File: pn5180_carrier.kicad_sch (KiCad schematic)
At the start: 35 parts, among them J1 Bay 0 (CLIK-Mate 1x10), J10 24V IN (CLIK-Mate 1x2), J2 Bay 1 (CLIK-Mate 1x10), J3 Bay 2 (CLIK-Mate 1x10), J4 Bay 3 (CLIK-Mate 1x10), J5 Bay 4 (CLIK-Mate 1x10), J6 Bay 5 (CLIK-Mate 1x10), J7 Bay 6 (CLIK-Mate 1x10), J8 Bay 7 (CLIK-Mate 1x10), U1 74HC138, U2 74HC151, U4 TLV1117LV33DCYR, U5 XIAO ESP32C6, U6 MP1584EN module (set 5.0V)

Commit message: Bay connectors J1-J8: CLIK-Mate 1.50 mm dual-row 2x5 (503148-1090), rev 1.4
- New project footprint carrier:Molex_CLIK-Mate_503148-1090_2x05-1MP_P1.50mm_Horizontal
  from Molex's catalog drawing (10 pads 0.55x2.70 at 0.75 mm in one line at the rear,
  nail pads 1.20x4.65 at the front corners, body 11.8x8.75). Nail-pad fore-aft position
  and the sequential pad order are to be confirmed on SD-503148-1090.
- Schematic: J1-J8 footprint/MPN/Mouser/description/value fields, DESIGN NOTES text,
  title-block rev 1.3 -> 1.4. Netlist (38 nets, 189 nodes, 0 problems) and ERC unchanged.
- BOM CSV and Mouser order list: 503148-1090 x8, housing 503149-1000 x8, terminals
  502579-0000 cut strip of 100; the 24 V cable stays on the 2.00 mm family.
- README, CLAUDE.md, MEMORY.md: connector, harness (24-28 AWG thin-wall), stock check,
  layout consequences; PCB footprint swap and re-layout recorded as open item 12.

Co-Authored-By: Claude Fable 5.1 <noreply@anthropic.com>
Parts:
- J1: value Bay 0 (CLIK-Mate 1x10) -> Bay 0 (CLIK-Mate 2x5); footprint Connector_Molex:Molex_CLIK-Mate_502494-1070_1x10-1MP_P2.00mm_Horizontal -> carrier:Molex_CLIK-Mate_503148-1090_2x05-1MP_P1.50mm_Horizontal; MPN 502494-1070 -> 503148-1090; Mouser 538-502494-1070 -> 538-503148-1090
- J2: value Bay 1 (CLIK-Mate 1x10) -> Bay 1 (CLIK-Mate 2x5); footprint Connector_Molex:Molex_CLIK-Mate_502494-1070_1x10-1MP_P2.00mm_Horizontal -> carrier:Molex_CLIK-Mate_503148-1090_2x05-1MP_P1.50mm_Horizontal; MPN 502494-1070 -> 503148-1090; Mouser 538-502494-1070 -> 538-503148-1090
- J3: value Bay 2 (CLIK-Mate 1x10) -> Bay 2 (CLIK-Mate 2x5); footprint Connector_Molex:Molex_CLIK-Mate_502494-1070_1x10-1MP_P2.00mm_Horizontal -> carrier:Molex_CLIK-Mate_503148-1090_2x05-1MP_P1.50mm_Horizontal; MPN 502494-1070 -> 503148-1090; Mouser 538-502494-1070 -> 538-503148-1090
- J4: value Bay 3 (CLIK-Mate 1x10) -> Bay 3 (CLIK-Mate 2x5); footprint Connector_Molex:Molex_CLIK-Mate_502494-1070_1x10-1MP_P2.00mm_Horizontal -> carrier:Molex_CLIK-Mate_503148-1090_2x05-1MP_P1.50mm_Horizontal; MPN 502494-1070 -> 503148-1090; Mouser 538-502494-1070 -> 538-503148-1090
- J5: value Bay 4 (CLIK-Mate 1x10) -> Bay 4 (CLIK-Mate 2x5); footprint Connector_Molex:Molex_CLIK-Mate_502494-1070_1x10-1MP_P2.00mm_Horizontal -> carrier:Molex_CLIK-Mate_503148-1090_2x05-1MP_P1.50mm_Horizontal; MPN 502494-1070 -> 503148-1090; Mouser 538-502494-1070 -> 538-503148-1090
- J6: value Bay 5 (CLIK-Mate 1x10) -> Bay 5 (CLIK-Mate 2x5); footprint Connector_Molex:Molex_CLIK-Mate_502494-1070_1x10-1MP_P2.00mm_Horizontal -> carrier:Molex_CLIK-Mate_503148-1090_2x05-1MP_P1.50mm_Horizontal; MPN 502494-1070 -> 503148-1090; Mouser 538-502494-1070 -> 538-503148-1090
- J7: value Bay 6 (CLIK-Mate 1x10) -> Bay 6 (CLIK-Mate 2x5); footprint Connector_Molex:Molex_CLIK-Mate_502494-1070_1x10-1MP_P2.00mm_Horizontal -> carrier:Molex_CLIK-Mate_503148-1090_2x05-1MP_P1.50mm_Horizontal; MPN 502494-1070 -> 503148-1090; Mouser 538-502494-1070 -> 538-503148-1090
- J8: value Bay 7 (CLIK-Mate 1x10) -> Bay 7 (CLIK-Mate 2x5); footprint Connector_Molex:Molex_CLIK-Mate_502494-1070_1x10-1MP_P2.00mm_Horizontal -> carrier:Molex_CLIK-Mate_503148-1090_2x05-1MP_P1.50mm_Horizontal; MPN 502494-1070 -> 503148-1090; Mouser 538-502494-1070 -> 538-503148-1090
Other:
- note added: "All SMD except the XIAO sockets and U6's four THT pads. Bays: Molex CLIK-Mate 1.50mm dual-row RA receptacles 503148-1090 (2x5), housings 503149-1000, terminals 502579 (24-28 AWG). J10: CLIK-Mate 2.00mm 502494-0270, housing 502439-0200, terminals 502438."
- note removed: "All SMD except the XIAO sockets. Connectors: Molex CLIK-Mate 2.00mm RA receptacles (502494-xx70), housings 502439-xx00, terminals 502438."
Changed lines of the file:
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@@
 		(title "PN5180 8-Bay NFC Reader Carrier")
 		(date "2026-09-04")
-		(rev "1.3")
+		(rev "1.4")
 		(company "hyiger")
 		(comment 1 "74HC138 chip-select decoder + 74HC151 BUSY mux, 5 ESP32 GPIOs for 8 readers")
@@
 		)
 	)
-	(text "All SMD except the XIAO sockets. Connectors: Molex CLIK-Mate 2.00mm RA receptacles (502494-xx70), housings 502439-xx00, terminals 502438."
+	(text "All SMD except the XIAO sockets and U6's four THT pads. Bays: Molex CLIK-Mate 1.50mm dual-row RA receptacles 503148-1090 (2x5), housings 503149-1000, terminals 502579 (24-28 AWG). J10: CLIK-Mate 2.00mm 502494-0270, housing 502439-0200, terminals 502438."
 		(exclude_from_sim no)
 		(at 243.84 226.06 0)
@@
 			)
 		)
-		(property "Value" "Bay 1 (CLIK-Mate 1x10)"
+		(property "Value" "Bay 1 (CLIK-Mate 2x5)"
 			(at 266.7 95.885 0)
 			(show_name no)
@@
 			)
 		)
-		(property "Footprint" "Connector_Molex:Molex_CLIK-Mate_502494-1070_1x10-1MP_P2.00mm_Horizontal"
+		(property "Footprint" "carrier:Molex_CLIK-Mate_503148-1090_2x05-1MP_P1.50mm_Horizontal"
 			(at 269.24 81.28 0)
 			(hide yes)
@@
 			)
 		)
-		(property "Description" "CLIK-Mate 2.00mm RA SMT receptacle 1x10, positive lock"
+		(property "Description" "CLIK-Mate 1.50mm dual-row RA SMT receptacle 2x5, positive lock"
 			(at 269.24 81.28 0)
 			(hide yes)
@@
 			)
 		)
-		(property "MPN" "502494-1070"
+		(property "MPN" "503148-1090"
 			(at 269.24 81.28 0)
 			(hide yes)
@@
 			)
 		)
-		(property "Mouser" "538-502494-1070"
+		(property "Mouser" "538-503148-1090"
 			(at 269.24 81.28 0)
 			(hide yes)
@@
 			)
 		)
-		(property "Value" "Bay 5 (CLIK-Mate 1x10)"
+		(property "Value" "Bay 5 (CLIK-Mate 2x5)"
 			(at 353.06 95.885 0)
 			(show_name no)
@@
 			)
 		)
-		(property "Footprint" "Connector_Molex:Molex_CLIK-Mate_502494-1070_1x10-1MP_P2.00mm_Horizontal"
+		(property "Footprint" "carrier:Molex_CLIK-Mate_503148-1090_2x05-1MP_P1.50mm_Horizontal"
 			(at 355.6 81.28 0)
 			(hide yes)
@@
 			)
 		)
-		(property "Description" "CLIK-Mate 2.00mm RA SMT receptacle 1x10, positive lock"
+		(property "Description" "CLIK-Mate 1.50mm dual-row RA SMT receptacle 2x5, positive lock"
 			(at 355.6 81.28 0)
 			(hide yes)
@@
 			)
 		)
-		(property "MPN" "502494-1070"
+		(property "MPN" "503148-1090"
 			(at 355.6 81.28 0)
 			(hide yes)
@@
 			)
 		)
-		(property "Mouser" "538-502494-1070"
+		(property "Mouser" "538-503148-1090"
 			(at 355.6 81.28 0)
 			(hide yes)
@@
 			)
 		)
-		(property "Value" "Bay 6 (CLIK-Mate 1x10)"
+		(property "Value" "Bay 6 (CLIK-Mate 2x5)"
 			(at 353.06 136.525 0)
 			(show_name no)
@@
 			)
 		)
-		(property "Footprint" "Connector_Molex:Molex_CLIK-Mate_502494-1070_1x10-1MP_P2.00mm_Horizontal"
+		(property "Footprint" "carrier:Molex_CLIK-Mate_503148-1090_2x05-1MP_P1.50mm_Horizontal"
 			(at 355.6 121.92 0)
 			(hide yes)
@@
 			)
 		)
-		(property "Description" "CLIK-Mate 2.00mm RA SMT receptacle 1x10, positive lock"
+		(property "Description" "CLIK-Mate 1.50mm dual-row RA SMT receptacle 2x5, positive lock"
 			(at 355.6 121.92 0)
 			(hide yes)
@@
 			)
 		)
-		(property "MPN" "502494-1070"
+		(property "MPN" "503148-1090"
 			(at 355.6 121.92 0)
 			(hide yes)
@@
 			)
 		)
-		(property "Mouser" "538-502494-1070"
+		(property "Mouser" "538-503148-1090"
 			(at 355.6 121.92 0)
 			(hide yes)
@@
 			)
 		)
-		(property "Value" "Bay 7 (CLIK-Mate 1x10)"
+		(property "Value" "Bay 7 (CLIK-Mate 2x5)"
 			(at 353.06 177.165 0)
 			(show_name no)
@@
 			)
 		)
-		(property "Footprint" "Connector_Molex:Molex_CLIK-Mate_502494-1070_1x10-1MP_P2.00mm_Horizontal"
+		(property "Footprint" "carrier:Molex_CLIK-Mate_503148-1090_2x05-1MP_P1.50mm_Horizontal"
 			(at 355.6 162.56 0)
 			(hide yes)
@@
 			)
 		)
-		(property "Description" "CLIK-Mate 2.00mm RA SMT receptacle 1x10, positive lock"
+		(property "Description" "CLIK-Mate 1.50mm dual-row RA SMT receptacle 2x5, positive lock"
 			(at 355.6 162.56 0)
 			(hide yes)
@@
 			)
 		)
-		(property "MPN" "502494-1070"
+		(property "MPN" "503148-1090"
 			(at 355.6 162.56 0)
 			(hide yes)
@@
 			)
 		)
-		(property "Mouser" "538-502494-1070"
+		(property "Mouser" "538-503148-1090"
 			(at 355.6 162.56 0)
 			(hide yes)
@@
 			)
 		)
-		(property "Value" "Bay 0 (CLIK-Mate 1x10)"
+		(property "Value" "Bay 0 (CLIK-Mate 2x5)"
 			(at 266.7 55.245 0)
 			(show_name no)
@@
 			)
 		)
-		(property "Footprint" "Connector_Molex:Molex_CLIK-Mate_502494-1070_1x10-1MP_P2.00mm_Horizontal"
+		(property "Footprint" "carrier:Molex_CLIK-Mate_503148-1090_2x05-1MP_P1.50mm_Horizontal"
 			(at 269.24 40.64 0)
 			(hide yes)
@@
 			)
 		)
-		(property "Description" "CLIK-Mate 2.00mm RA SMT receptacle 1x10, positive lock"
+		(property "Description" "CLIK-Mate 1.50mm dual-row RA SMT receptacle 2x5, positive lock"
 			(at 269.24 40.64 0)
 			(hide yes)
@@
 			)
 		)
-		(property "MPN" "502494-1070"
+		(property "MPN" "503148-1090"
 			(at 269.24 40.64 0)
 			(hide yes)
@@
 			)
 		)
-		(property "Mouser" "538-502494-1070"
+		(property "Mouser" "538-503148-1090"
 			(at 269.24 40.64 0)
 			(hide yes)
@@
 			)
 		)
-		(property "Value" "Bay 3 (CLIK-Mate 1x10)"
+		(property "Value" "Bay 3 (CLIK-Mate 2x5)"
 			(at 266.7 177.165 0)
 			(show_name no)
@@
 			)
 		)
-		(property "Footprint" "Connector_Molex:Molex_CLIK-Mate_502494-1070_1x10-1MP_P2.00mm_Horizontal"
+		(property "Footprint" "carrier:Molex_CLIK-Mate_503148-1090_2x05-1MP_P1.50mm_Horizontal"
 			(at 269.24 162.56 0)
 			(hide yes)
@@
 			)
 		)
-		(property "Description" "CLIK-Mate 2.00mm RA SMT receptacle 1x10, positive lock"
+		(property "Description" "CLIK-Mate 1.50mm dual-row RA SMT receptacle 2x5, positive lock"
 			(at 269.24 162.56 0)
 			(hide yes)
@@
 			)
 		)
-		(property "MPN" "502494-1070"
+		(property "MPN" "503148-1090"
 			(at 269.24 162.56 0)
 			(hide yes)
@@
 			)
 		)
-		(property "Mouser" "538-502494-1070"
+		(property "Mouser" "538-503148-1090"
 			(at 269.24 162.56 0)
 			(hide yes)
@@
 			)
 		)
-		(property "Value" "Bay 2 (CLIK-Mate 1x10)"
+		(property "Value" "Bay 2 (CLIK-Mate 2x5)"
 			(at 266.7 136.525 0)
 			(show_name no)
@@
 			)
 		)
-		(property "Footprint" "Connector_Molex:Molex_CLIK-Mate_502494-1070_1x10-1MP_P2.00mm_Horizontal"
+		(property "Footprint" "carrier:Molex_CLIK-Mate_503148-1090_2x05-1MP_P1.50mm_Horizontal"
 			(at 269.24 121.92 0)
 			(hide yes)
@@
 			)
 		)
-		(property "Description" "CLIK-Mate 2.00mm RA SMT receptacle 1x10, positive lock"
+		(property "Description" "CLIK-Mate 1.50mm dual-row RA SMT receptacle 2x5, positive lock"
 			(at 269.24 121.92 0)
 			(hide yes)
@@
 			)
 		)
-		(property "MPN" "502494-1070"
+		(property "MPN" "503148-1090"
 			(at 269.24 121.92 0)
 			(hide yes)
@@
 			)
 		)
-		(property "Mouser" "538-502494-1070"
+		(property "Mouser" "538-503148-1090"
 			(at 269.24 121.92 0)
 			(hide yes)
@@
 			)
 		)
-		(property "Value" "Bay 4 (CLIK-Mate 1x10)"
+		(property "Value" "Bay 4 (CLIK-Mate 2x5)"
 			(at 353.06 55.245 0)
 			(show_name no)
@@
 			)
 		)
-		(property "Footprint" "Connector_Molex:Molex_CLIK-Mate_502494-1070_1x10-1MP_P2.00mm_Horizontal"
+		(property "Footprint" "carrier:Molex_CLIK-Mate_503148-1090_2x05-1MP_P1.50mm_Horizontal"
 			(at 355.6 40.64 0)
 			(hide yes)
@@
 			)
 		)
-		(property "Description" "CLIK-Mate 2.00mm RA SMT receptacle 1x10, positive lock"
+		(property "Description" "CLIK-Mate 1.50mm dual-row RA SMT receptacle 2x5, positive lock"
 			(at 355.6 40.64 0)
 			(hide yes)
@@
 			)
 		)
-		(property "MPN" "502494-1070"
+		(property "MPN" "503148-1090"
 			(at 355.6 40.64 0)
 			(hide yes)
@@
 			)
 		)
-		(property "Mouser" "538-502494-1070"
+		(property "Mouser" "538-503148-1090"
 			(at 355.6 40.64 0)
 			(hide yes)

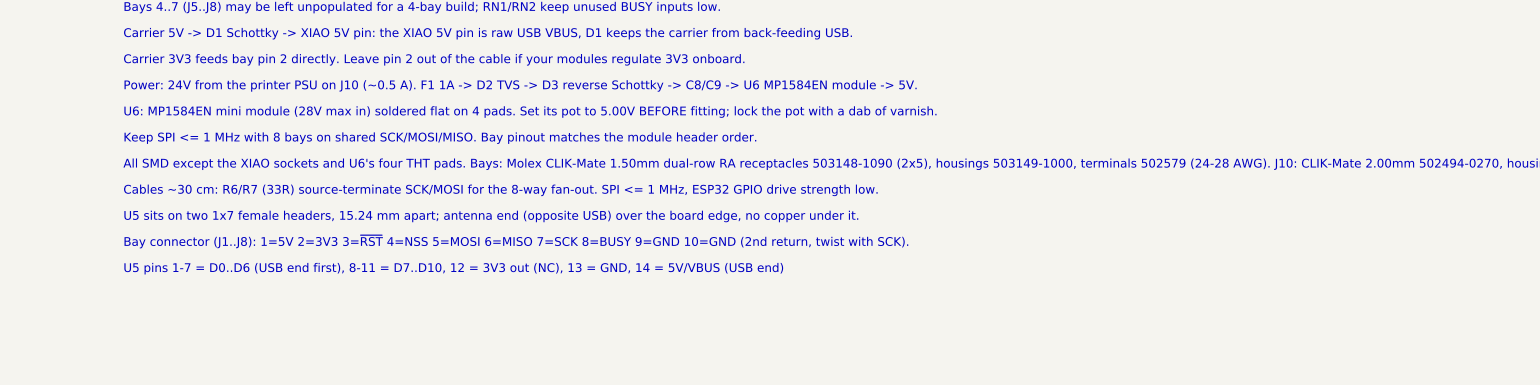
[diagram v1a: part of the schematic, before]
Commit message: 2x5 connector: footprint corrections from the verification pass, doc fixes
- Footprint: pad line offset 0.375 mm toward pin 10 (pads +3.0 .. -3.75), nail pads
  moved to the mating-face datum (centre Y +2.05), courtyard front to +5.0, silk stub
  and pin-1 triangle adjusted, descr rewritten. Scratch DRC with the project rules: 0.
- Schematic: U5 note (USB end at the edge, antenna inboard), title-block date 2026-09-05,
  comment 2 reworded; renders re-exported. Netlist and ERC unchanged.
- README: PCB/gerbers still carry the 1x10 parts; cable build by circuit number with the
  pairing marked as inferred; terminal insulation range 0.78-1.28 mm; crimper guidance;
  old 1x10 length 24.0 mm; distributor snapshot stated as seen.
- CLAUDE.md/MEMORY.md: pre-swap figures marked, footprint notes updated, F1 fuse family
  (NANO2 451/453 is fast-acting, not Slo-Blo) raised as open item 13.

Co-Authored-By: Claude Fable 5.1 <noreply@anthropic.com>
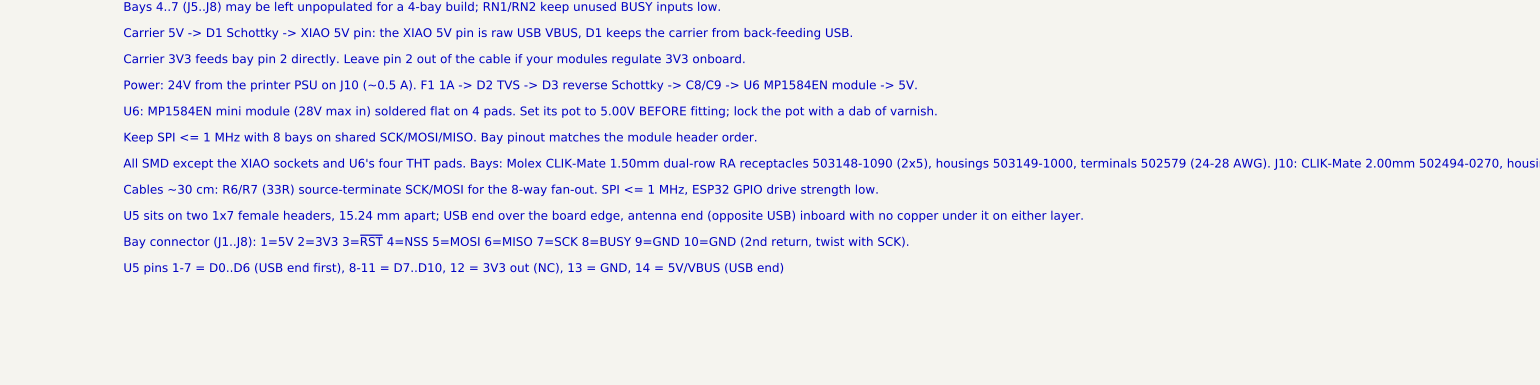
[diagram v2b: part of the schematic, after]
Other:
- note added: "U5 sits on two 1x7 female headers, 15.24 mm apart; USB end over the board edge, antenna end (opposite USB) inboard with no copper under it on either layer."
- note removed: "U5 sits on two 1x7 female headers, 15.24 mm apart; antenna end (opposite USB) over the board edge, no copper under it."
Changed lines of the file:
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@@
 	(title_block
 		(title "PN5180 8-Bay NFC Reader Carrier")
-		(date "2026-09-04")
+		(date "2026-09-05")
 		(rev "1.4")
 		(company "hyiger")
 		(comment 1 "74HC138 chip-select decoder + 74HC151 BUSY mux, 5 ESP32 GPIOs for 8 readers")
-		(comment 2 "Generated with gen_kicad.py")
+		(comment 2 "Originally generated with gen_kicad.py; hand-edited in KiCad 10 since rev 1.3")
 	)
-	(text "U5 sits on two 1x7 female headers, 15.24 mm apart; antenna end (opposite USB) over the board edge, no copper under it."
+	(text "U5 sits on two 1x7 female headers, 15.24 mm apart; USB end over the board edge, antenna end (opposite USB) inboard with no copper under it on either layer."
 		(exclude_from_sim no)
 		(at 243.84 233.68 0)
